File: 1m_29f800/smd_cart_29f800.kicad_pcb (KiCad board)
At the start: 2 copper layers, 83.8 x 40 mm, 16 parts, among them CON1 smd_cart_connector_edge, U1 74HCT00, U2 29f800-TSOP48, U3 29f800-SOP44

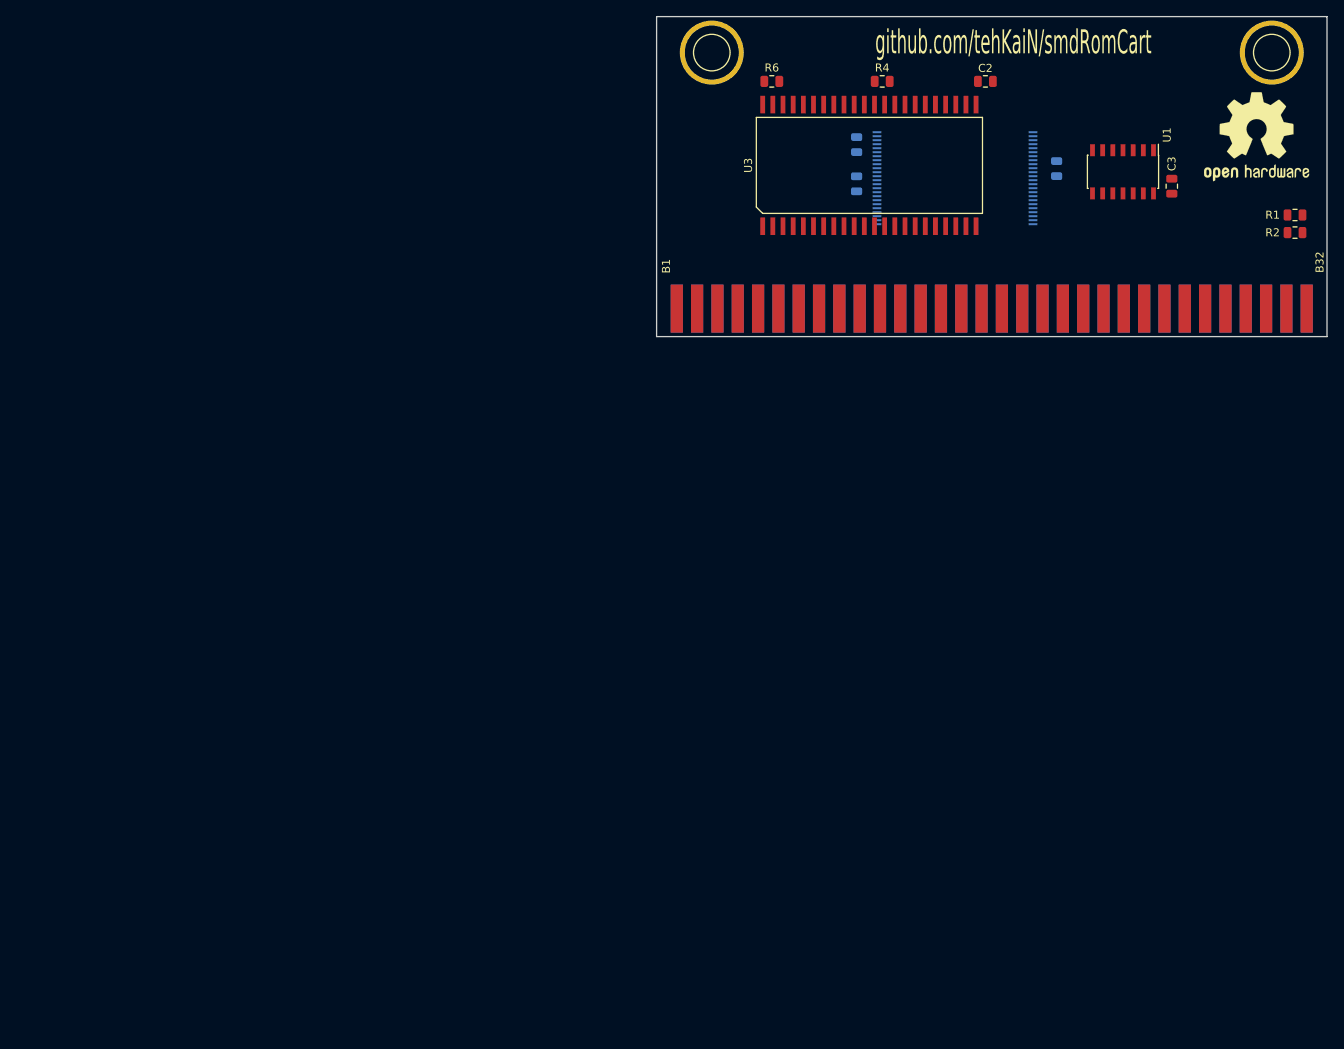
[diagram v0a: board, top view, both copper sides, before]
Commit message: fixed library paths
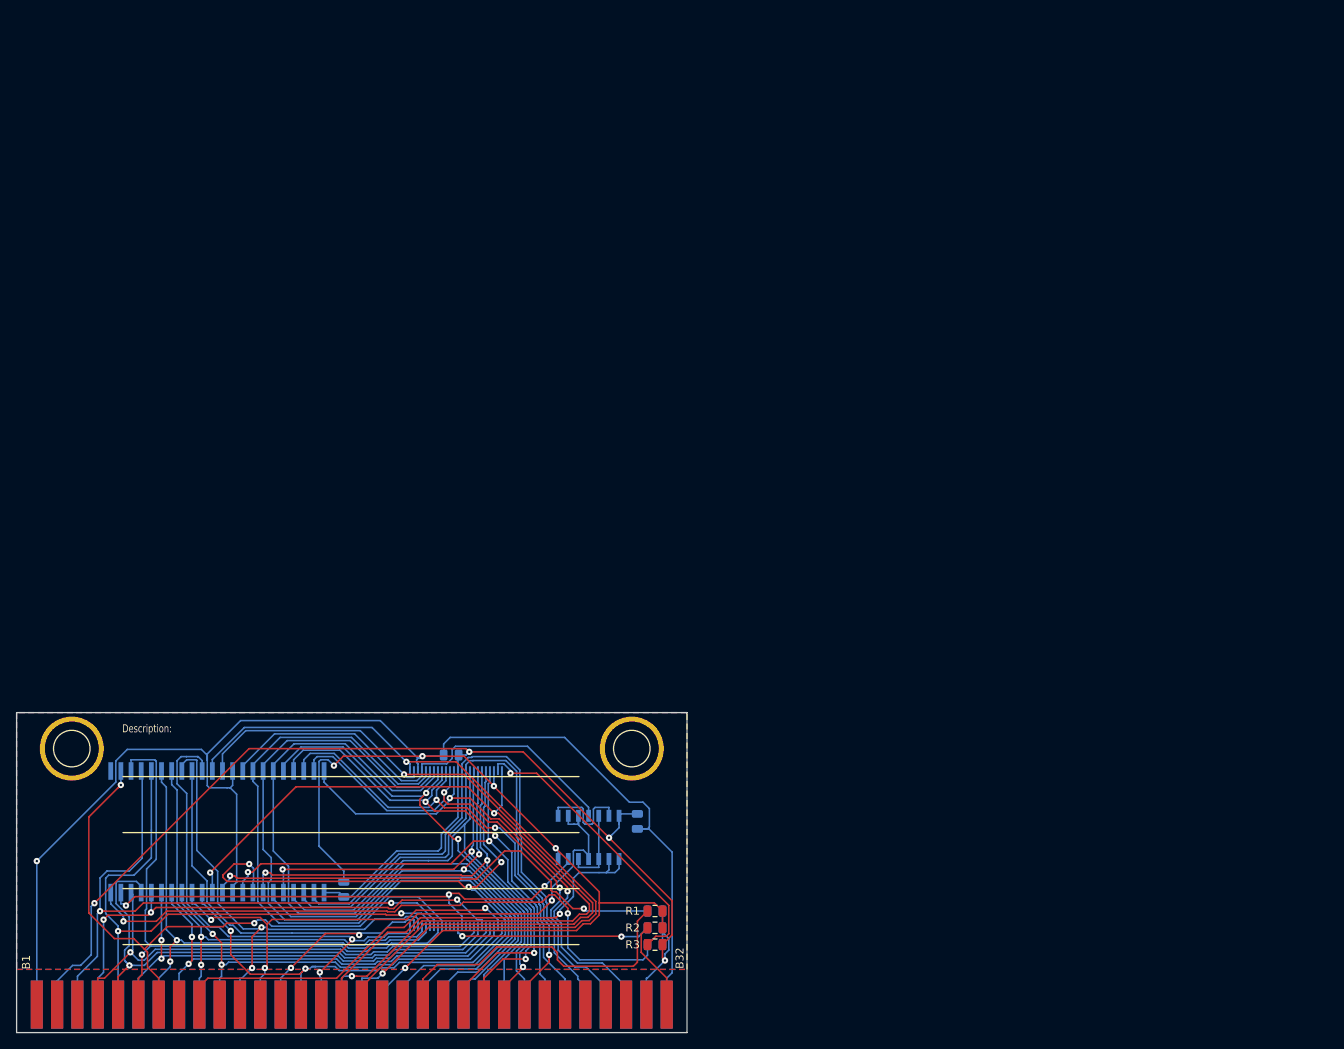
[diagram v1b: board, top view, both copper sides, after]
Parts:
- C2, C3, R4, R6, REF**, U1, U3: moved to B.Cu
- R3: moved to F.Cu
- moved REF** 130.4 mm to (132.1, 170.5), turned to 180 degrees
- moved R1 118.2 mm to (143.5, 169.8)
- moved CON1 118.2 mm to (66.2, 181.5)
- moved DRL1 118.2 mm to (140.6, 149.5)
- moved DRL2 118.2 mm to (70.6, 149.5)
- moved R2 118.1 mm to (143.5, 171.9)
- moved U3 116.5 mm to (88.8, 159.9)
- moved C1 109.0 mm to (104.6, 167.1), turned to 90 degrees
- moved R6 108.9 mm to (143.5, 174.0)
- moved R4 107.5 mm to (143.5, 169.8)
- moved C2 107.5 mm to (118.0, 150.3), turned to 180 degrees
- moved R5 107.4 mm to (143.5, 171.9), turned to 180 degrees
- moved U1 106.7 mm to (135.2, 160.6), turned to 90 degrees
- moved U2 104.5 mm to (118.6, 162.0), turned to 90 degrees
- moved C3 103.8 mm to (141.3, 158.6), turned to 270 degrees
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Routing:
- net GND: track 0.00 -> 274.1 mm, vias 0 -> 6
- net +5V: track 0.00 -> 165.0 mm, vias 0 -> 4
- net /A16: track 0.00 -> 104.9 mm, vias 0 -> 3
- net /A0: track 0.00 -> 98.9 mm, vias 0 -> 2
- net /D0: track 0.00 -> 98.3 mm
- net ~CE: track 0.00 -> 96.9 mm, vias 0 -> 1
- net /D8: track 0.00 -> 95.2 mm
- net /D1: track 0.00 -> 90.7 mm
- net /D7: track 0.00 -> 82.9 mm, vias 0 -> 3
- net Net-(R6-Pad2): track 0.00 -> 79.0 mm, vias 0 -> 2
- net /A18: track 0.00 -> 78.4 mm, vias 0 -> 2
- net /A7: track 0.00 -> 78.1 mm, vias 0 -> 2
- net /A6: track 0.00 -> 75.1 mm, vias 0 -> 2
- net /A17: track 0.00 -> 74.4 mm, vias 0 -> 1
- net /D12: track 0.00 -> 73.4 mm, vias 0 -> 1
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- added copper zone on B.Cu, net GND
- added copper zone on F.Cu, net GND
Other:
- board text added: "Description:"
- board text added: "MegaDrive ROM cart 1M Rev. 1"
- board text added: "github.com/tehKaiN/smdCart"
- board text removed: "MegaDrive ROM cart 512k + DBG Rev. 1"
- board text removed: "github.com/tehKaiN/smdRomCart"
